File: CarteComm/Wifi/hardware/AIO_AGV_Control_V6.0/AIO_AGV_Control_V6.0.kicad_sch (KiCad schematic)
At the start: 57 parts, among them J1 DB25_Pins, J2 DB25_Socket, T1 IRF520, T10 IRF520, T11 IRF520, T12 IRF520, T14 IRF520, T15 IRF520, T16 IRF520, T17 IRF520, T18 IRF520, T19 IRF520, T2 IRF520, T20 IRF520, T21 IRF520, T22 IRF520, T23 IRF520, T24 IRF520, T3 IRF520, T4 IRF520, T5 IRF520, T6 IRF520, T7 IRF520, T8 IRF520, T9 IRF520, U1 ESP32-DEVKITC

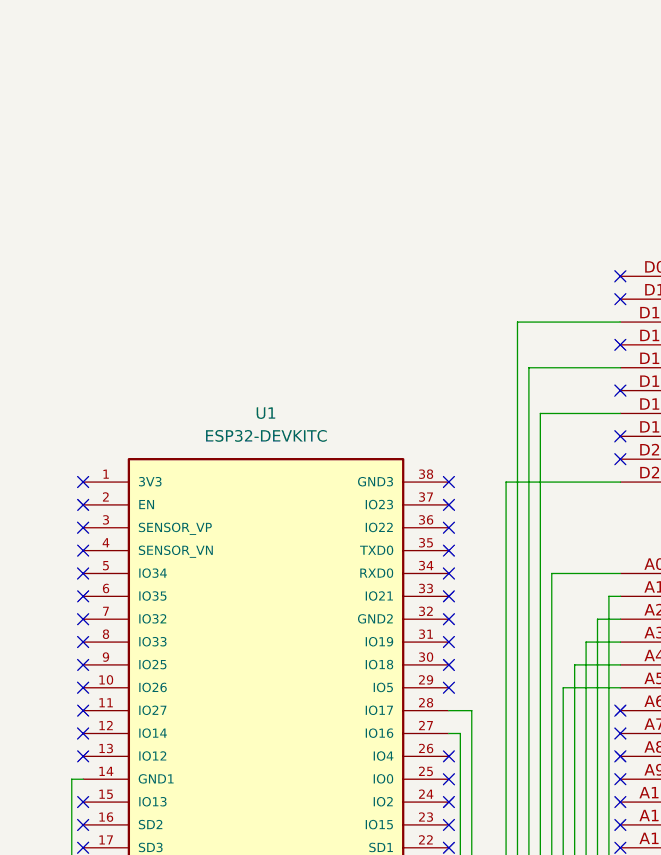
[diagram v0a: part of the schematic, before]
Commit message: feat(bom): resserrer les nomenclatures sur les composants déterminants
Les accessoires arbitrables selon le budget - antennes, boîtiers, coffrets,
enveloppes murales, câbles, plaques gravées - sortent de l'affichage et des
sous-totaux. Trente-six lignes qui se substituent librement d'un fournisseur à
l'autre et n'engagent aucun choix de conception : elles allongeaient la lecture
sans rien apporter à la décision.

Elles restent définies dans generer_bom.py, marquées core=False. Rien n'est
perdu, et un accessoire redevient visible en changeant un mot.

Chaque BOM s'ouvre désormais sur un bloc Total, par variante, avec une colonne
rappelant le montant des accessoires écartés. Sans ce rappel, un total amputé
des antennes et des boîtiers se lirait comme un coût d'achat complet.

Deux effets de bord traités plutôt que laissés passer. Le point de bascule
A1/A3 se calculait sur des boutons dont le prix tient justement au boîtier IP65
et au poussoir Ø22 : retirer ces lignes inversait le classement. Ce tableau
raisonne donc accessoires compris, le dit, et le point de bascule est maintenant
CALCULÉ au lieu d'être asséné - il passe de 8 à 9 stations. Deux coûts par
station encore codés en dur à 50 EUR ont été branchés sur les sections.

README.md et COMPARAISON.md gardent la base complète, pour la même raison :
comparer des architectures sans leurs boîtiers fausserait le classement. Leurs
chiffres sont plus élevés que ceux des BOM, et les deux documents le disent.
Deux totaux LoRa y étaient restés périmés depuis la réutilisation de la carte
V5.0.1 - corrigés à 208 et 307 EUR.

Contrôle : core + accessoires retombe exactement sur les six totaux complets
cités par les documents de comparaison.

Co-Authored-By: Claude Opus 5 <noreply@anthropic.com>
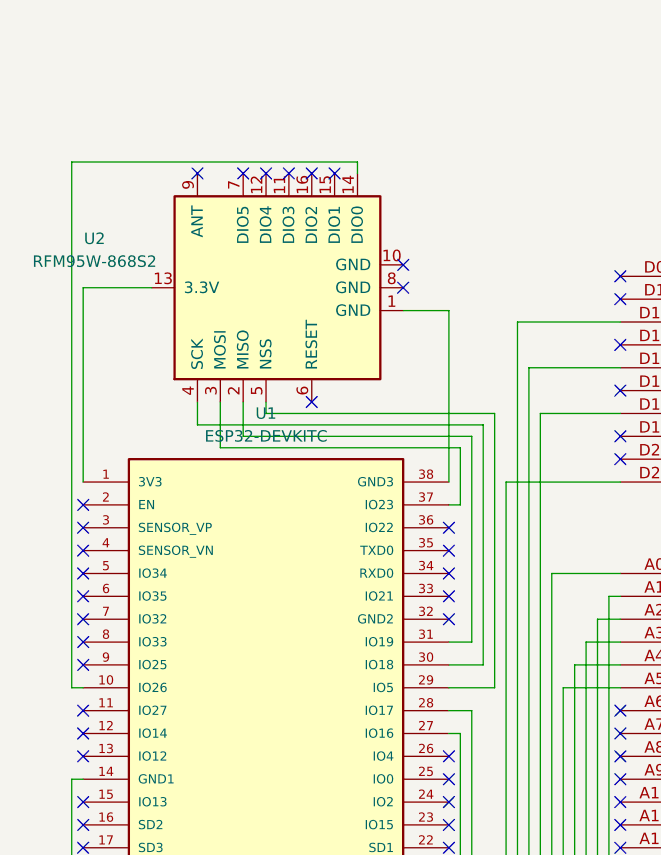
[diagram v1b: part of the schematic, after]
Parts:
- added U2: RFM95W-868S2, RF_Module:HOPERF_RFM9XW_SMD, symbol RF_Module:RFM95W-868S2
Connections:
- net at U1.1 (3V3): now also U2.13 (3.3V)
- net at U1.10 (IO26): now also U2.14 (DIO0)
- net at U1.29 (IO5): now also U2.5 (NSS)
- net at U1.30 (IO18): now also U2.4 (SCK)
- net at U1.31 (IO19): now also U2.2 (MISO)
- net at U1.37 (IO23): now also U2.3 (MOSI)
- net at U1.38 (GND3): now also U2.1 (GND)
- no-connect marks 71 -> 73
